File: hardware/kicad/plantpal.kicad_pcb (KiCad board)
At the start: 2 copper layers, 38.4 x 128.5 mm, 123 parts, among them J1 U262-161N-4BVC11, J2 +LIPO, J3 -LIPO, J4 687124182122, Q1 DMG1012UW, Q2 DMG3415U-7, Q3 MMBT3906, Q4 PMV32UP, Q5 DMG1012UW, Q6 AO3407A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

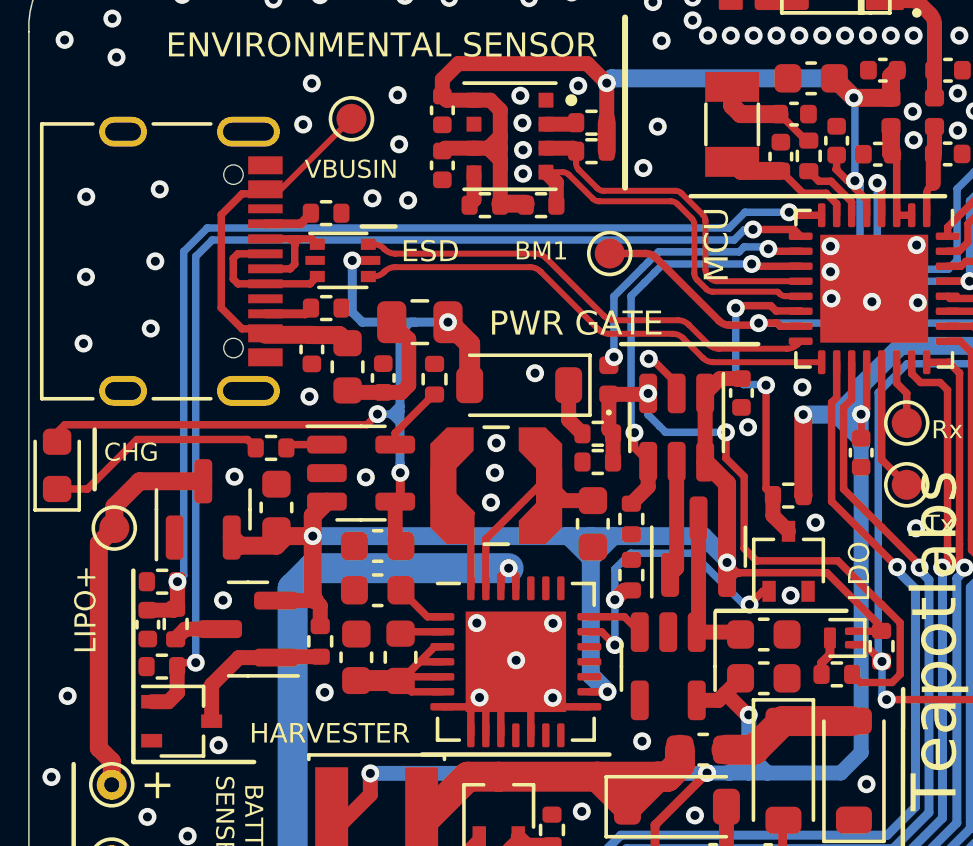
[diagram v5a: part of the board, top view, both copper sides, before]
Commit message: improve usb trace
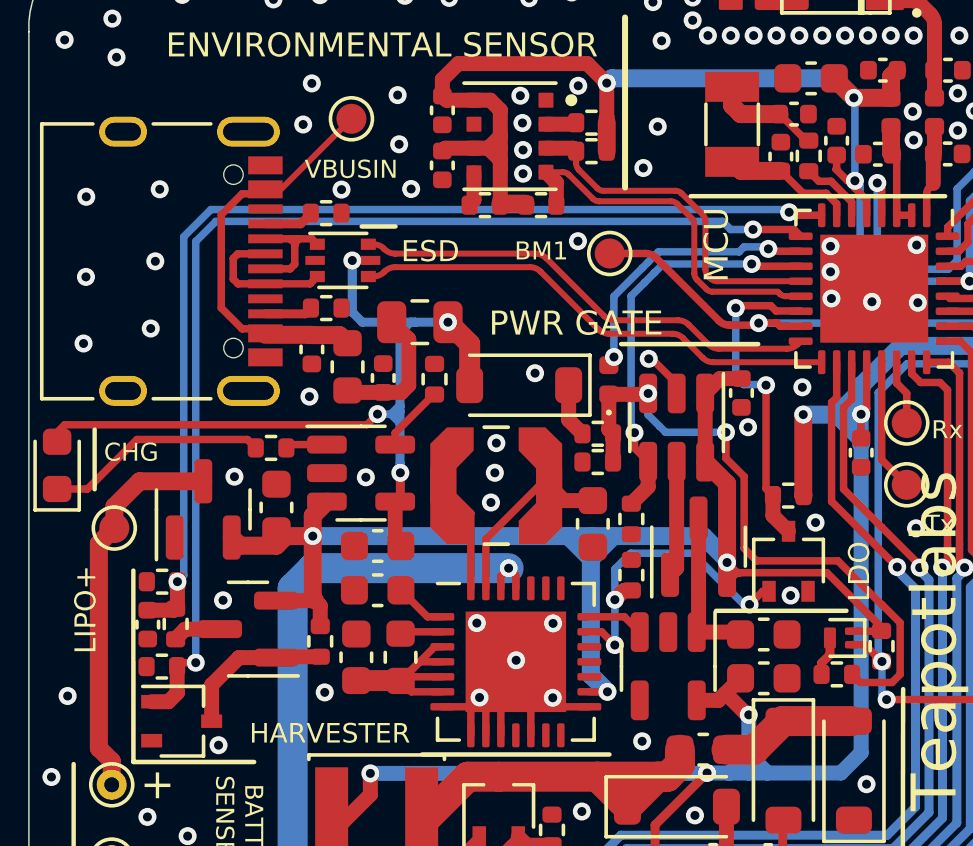
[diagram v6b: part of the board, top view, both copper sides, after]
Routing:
- net /Main Controller/BATT_MEAS_EN: track 36.7 -> 37.2 mm
- net GND: vias 184 -> 185
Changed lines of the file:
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@@
   (via (at 111.44 39.17) (size 0.6) (drill 0.3) (layers "F.Cu" "B.Cu") (free) (net 2))
   (via (at 99.83 48.17) (size 0.6) (drill 0.3) (layers "F.Cu" "B.Cu") (free) (net 2))
-  (via (at 101.93 41.56) (size 0.6) (drill 0.3) (layers "F.Cu" "B.Cu") (free) (net 2))
+  (via (at 100.9 41.27) (size 0.6) (drill 0.3) (layers "F.Cu" "B.Cu") (free) (net 2))
   (via (at 110.96 40.55) (size 0.6) (drill 0.3) (layers "F.Cu" "B.Cu") (free) (net 2))
   (via (at 104.49 34.88) (size 0.6) (drill 0.3) (layers "F.Cu" "B.Cu") (free) (net 2))
@@
   (via (at 106.72 56.96) (size 0.6) (drill 0.3) (layers "F.Cu" "B.Cu") (net 2))
   (via (at 120.07 43.12) (size 0.6) (drill 0.3) (layers "F.Cu" "B.Cu") (net 2))
-  (via (at 103.12 41.63) (size 0.6) (drill 0.3) (layers "F.Cu" "B.Cu") (free) (net 2))
+  (via (at 103.22 41.25) (size 0.6) (drill 0.3) (layers "F.Cu" "B.Cu") (free) (net 2))
   (via (at 100.34 58.03) (size 0.6) (drill 0.3) (layers "F.Cu" "B.Cu") (free) (net 2))
   (via (at 117.2 44.01) (size 0.6) (drill 0.3) (layers "F.Cu" "B.Cu") (net 2))
@@
   (via (at 104.82 69.22) (size 0.6) (drill 0.3) (layers "F.Cu" "B.Cu") (free) (net 2))
   (via (at 106.41 68.74) (size 0.6) (drill 0.3) (layers "F.Cu" "B.Cu") (free) (net 2))
+  (via (at 108.78 42.99) (size 0.6) (drill 0.3) (layers "F.Cu" "B.Cu") (free) (net 2))
   (via (at 106.95 39.95) (size 0.6) (drill 0.3) (layers "F.Cu" "B.Cu") (free) (net 2))
   (via (at 105.5 58.2) (size 0.6) (drill 0.3) (layers "F.Cu" "B.Cu") (net 2))
@@
   (via (at 95.43 54.34) (size 0.6) (drill 0.3) (layers "F.Cu" "B.Cu") (net 21))
   (segment (start 95.64 54.13) (end 95.43 54.34) (width 0.25) (layer "B.Cu") (net 21))
-  (segment (start 114.348035 42.025) (end 113.823535 42.5495) (width 0.25) (layer "B.Cu") (net 21))
-  (segment (start 115.82 42.0255) (end 115.8195 42.025) (width 0.25) (layer "B.Cu") (net 21))
-  (segment (start 95.64 43.334315) (end 95.64 54.13) (width 0.25) (layer "B.Cu") (net 21))
-  (segment (start 96.424814 42.5495) (end 95.64 43.334315) (width 0.25) (layer "B.Cu") (net 21))
-  (segment (start 113.823535 42.5495) (end 96.424814 42.5495) (width 0.25) (layer "B.Cu") (net 21))
-  (segment (start 115.8195 42.025) (end 114.348035 42.025) (width 0.25) (layer "B.Cu") (net 21))
+  (segment (start 96.546386 41.935) (end 95.64 42.841386) (width 0.25) (layer "B.Cu") (net 21))
+  (segment (start 115.82 42.0255) (end 115.7295 41.935) (width 0.25) (layer "B.Cu") (net 21))
+  (segment (start 115.7295 41.935) (end 96.546386 41.935) (width 0.25) (layer "B.Cu") (net 21))
+  (segment (start 95.64 42.841386) (end 95.64 54.13) (width 0.25) (layer "B.Cu") (net 21))
   (segment (start 123.9 51.05) (end 123.9 52.595) (width 0.25) (layer "F.Cu") (net 22))
   (segment (start 122.84 46.152072) (end 122.84 48.674398) (width 0.25) (layer "F.Cu") (net 22))
@@
   (via (at 96.04 57.04) (size 0.6) (drill 0.3) (layers "F.Cu" "B.Cu") (net 64))
   (via (at 114.61511 42.6) (size 0.6) (drill 0.3) (layers "F.Cu" "B.Cu") (net 64))
-  (segment (start 114.61511 42.6) (end 114.338721 42.6) (width 0.25) (layer "B.Cu") (net 64))
-  (segment (start 96.5905 42.9495) (end 96.04 43.5) (width 0.25) (layer "B.Cu") (net 64))
-  (segment (start 113.989221 42.9495) (end 96.5905 42.9495) (width 0.25) (layer "B.Cu") (net 64))
-  (segment (start 96.04 43.5) (end 96.04 57.04) (width 0.25) (layer "B.Cu") (net 64))
-  (segment (start 114.338721 42.6) (end 113.989221 42.9495) (width 0.25) (layer "B.Cu") (net 64))
+  (segment (start 96.71 42.33) (end 96.04 43) (width 0.25) (layer "B.Cu") (net 64))
+  (segment (start 96.04 43) (end 96.04 57.04) (width 0.25) (layer "B.Cu") (net 64))
+  (segment (start 113.87 42.6) (end 113.6 42.33) (width 0.25) (layer "B.Cu") (net 64))
+  (segment (start 113.6 42.33) (end 96.71 42.33) (width 0.25) (layer "B.Cu") (net 64))
+  (segment (start 114.61511 42.6) (end 113.87 42.6) (width 0.25) (layer "B.Cu") (net 64))
   (segment (start 121.78 43.026297) (end 121.78 42.413) (width 0.25) (layer "F.Cu") (net 65))
   (segment (start 121.482297 43.324) (end 121.78 43.026297) (width 0.25) (layer "F.Cu") (net 65))

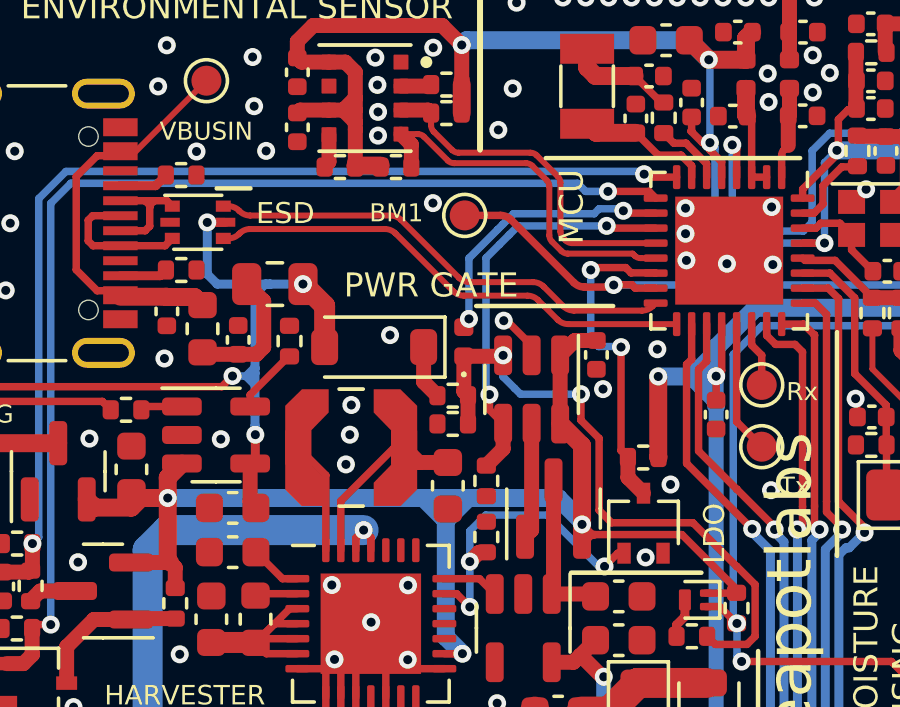
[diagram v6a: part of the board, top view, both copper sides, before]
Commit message: improve usb trace
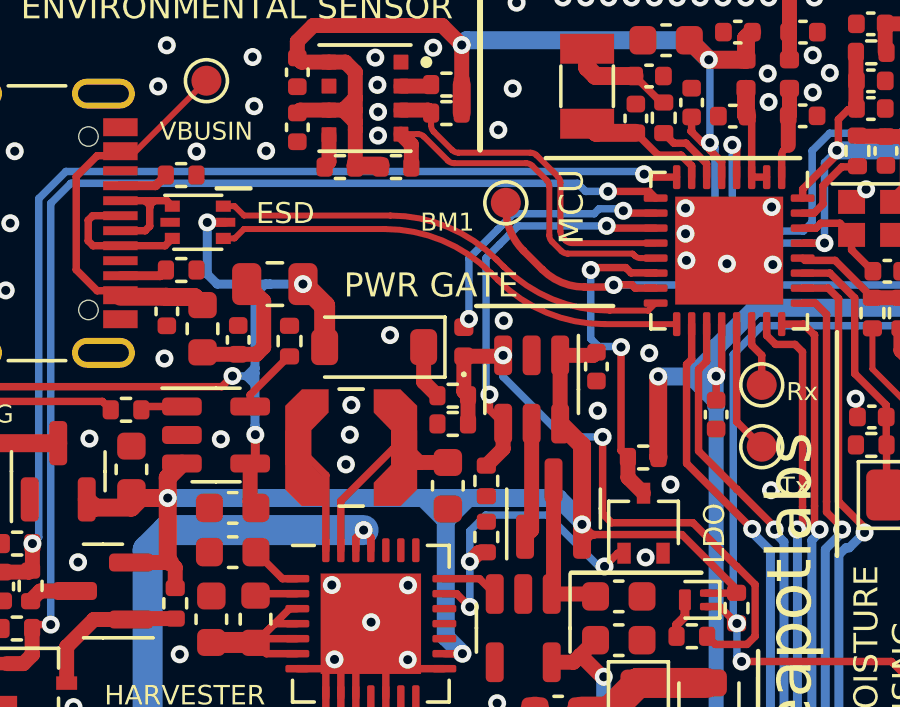
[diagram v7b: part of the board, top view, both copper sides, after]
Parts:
- moved TP7 1.43 mm to (111.2, 43.0)
- moved C24 0.39 mm to (114.2, 48.4)
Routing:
- net GND: track 21.0 -> 19.9 mm, vias 185 -> 184
- net /Main Controller/BOOT_MODE1: track 22.7 -> 22.0 mm
